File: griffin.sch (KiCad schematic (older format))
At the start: 43 parts, among them IC1 ME6211C33M5G-N, J1 USB_B_Micro, J2 Conn_02x03_Odd_Even, J3 Conn_01x04, J4 Conn_01x11, J5 Conn_01x04, J6 Conn_01x20, J7 Conn_01x20, J8 Conn_01x14, J9 Conn_01x08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

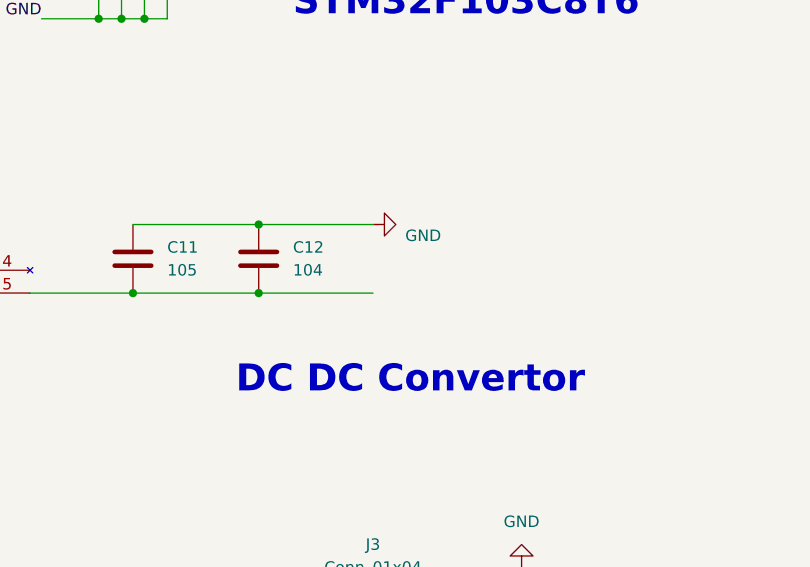
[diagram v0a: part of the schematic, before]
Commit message: remove _autosave-griffin.sch from .gitignore
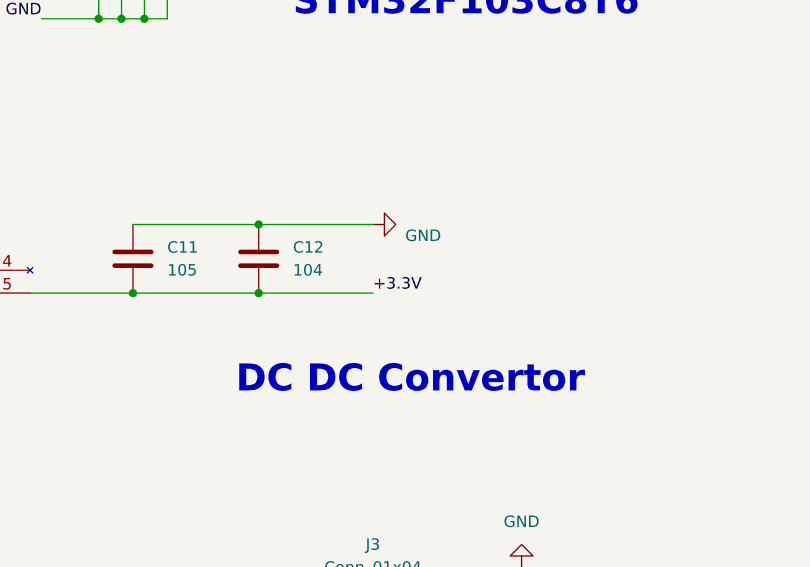
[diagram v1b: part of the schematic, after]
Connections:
- net +3.3V: now also C11.2, C12.2, IC1.5 (VOUT)
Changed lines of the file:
@@
 Text Label 8050 10600 0    50   ~ 0
 LED2
+Text Label 10000 8900 0    50   ~ 0
++3.3V
 $EndSCHEMATC

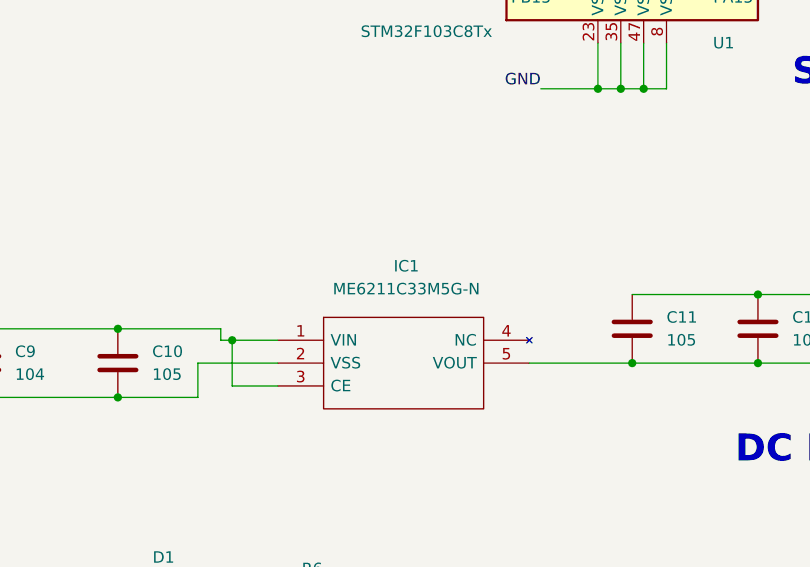
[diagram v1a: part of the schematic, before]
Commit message: adjust symbole libraries
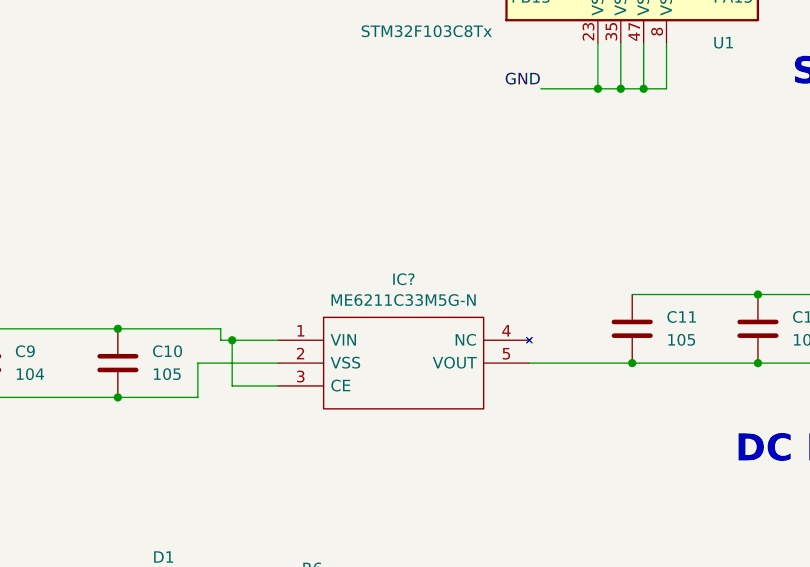
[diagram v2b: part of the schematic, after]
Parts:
- removed IC1: ME6211C33M5G-N, griffin:SOT95P270X145-5N, symbol ME6211C33M5G-N:ME6211C33M5G-N
- added IC?: ME6211C33M5G-N, SOT95P270X145-5N, symbol griffin:ME6211C33M5G-N
- SW3: footprint Button_Switch_THT:SW_PUSH-12mm -> Button_Switch_THT:SW_PUSH_6mm
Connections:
- net +3.3V: now also IC?.5 (VOUT)
- net GND: now also IC?.2 (VSS)
- net at C10.1, C9.1, F1.1: now also IC?.1 (VIN), IC?.3 (CE)
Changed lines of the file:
@@
 $EndDescr
-$Comp
-L ME6211C33M5G-N:ME6211C33M5G-N IC1
-U 1 1 605A15B8
-P 7400 8800
-F 0 "IC1" H 7962 9124 50  0000 C CNN
-F 1 "ME6211C33M5G-N" H 7962 9024 50  0000 C CNN
-F 2 "griffin:SOT95P270X145-5N" H 8350 8900 50  0001 L CNN
-F 3 "https://datasheet.lcsc.com/szlcsc/1811131510_MICRONE-Nanjing-Micro-One-Elec-ME6211C33M5G-N_C82942.pdf" H 8350 8800 50  0001 L CNN
-F 4 "Fixed 6V 3.3V 500mA SOT-23-5 Low Dropout Regulators(LDO) RoHS" H 8350 8700 50  0001 L CNN "Description"
-F 5 "1.45" H 8350 8600 50  0001 L CNN "Height"
-F 6 "Microne" H 8350 8500 50  0001 L CNN "Manufacturer_Name"
-F 7 "ME6211C33M5G-N" H 8350 8400 50  0001 L CNN "Manufacturer_Part_Number"
-F 8 "" H 8350 8300 50  0001 L CNN "Mouser Part Number"
-F 9 "" H 8350 8200 50  0001 L CNN "Mouser Price/Stock"
-F 10 "" H 8350 8100 50  0001 L CNN "Arrow Part Number"
-F 11 "" H 8350 8000 50  0001 L CNN "Arrow Price/Stock"
-	1    7400 8800
-	1    0    0    -1
-$EndComp
 $Comp
 L Device:R R1
@@
 F 0 "SW3" H 4650 2050 50  0000 C CNN
 F 1 "SW_Push" H 4650 1950 50  0000 C CNN
-F 2 "Button_Switch_THT:SW_PUSH-12mm" H 4650 1950 50  0001 C CNN
+F 2 "Button_Switch_THT:SW_PUSH_6mm" H 4650 1950 50  0001 C CNN
 F 3 "~" H 4650 1950 50  0001 C CNN
 	1    4650 1750
@@
 Text Label 10000 8900 0    50   ~ 0
 +3.3V
+$Comp
+L griffin:ME6211C33M5G-N IC?
+U 1 1 605ECAB2
+P 7400 8800
+F 0 "IC?" H 7950 9065 50  0000 C CNN
+F 1 "ME6211C33M5G-N" H 7950 8974 50  0000 C CNN
+F 2 "SOT95P270X145-5N" H 8350 8900 50  0001 L CNN
+F 3 "https://datasheet.lcsc.com/szlcsc/1811131510_MICRONE-Nanjing-Micro-One-Elec-ME6211C33M5G-N_C82942.pdf" H 8350 8800 50  0001 L CNN
+F 4 "Fixed 6V 3.3V 500mA SOT-23-5 Low Dropout Regulators(LDO) RoHS" H 8350 8700 50  0001 L CNN "Description"
+F 5 "1.45" H 8350 8600 50  0001 L CNN "Height"
+F 6 "Microne" H 8350 8500 50  0001 L CNN "Manufacturer_Name"
+F 7 "ME6211C33M5G-N" H 8350 8400 50  0001 L CNN "Manufacturer_Part_Number"
+	1    7400 8800
+	1    0    0    -1
+$EndComp
 $EndSCHEMATC

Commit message: finish PCB layout
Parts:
- removed P1: USB_C_Plug, Connector_USB:USB_C_Receptacle_Amphenol_12401610E4-2A, symbol Connector:USB_C_Plug
- removed SW3: SW_Push, Button_Switch_THT:SW_PUSH_6mm, symbol Switch:SW_Push
- gave numbers to parts that had none: 1
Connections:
- net +5V: now also J1.1 (VBUS)
- net D+: now reaches J1.3 (D+), R4.2
- net D+: no longer R3.2
- net D-: now reaches J1.2 (D-), R5.2
- net D-: now also R3.2
- no-connect marks 16 -> 4
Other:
- moved on the sheet: C10, C11, C12, C13, C14, C9, D1, D2, F1, IC1, J1, J2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
